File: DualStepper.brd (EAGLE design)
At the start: 53.1 x 63 mm, 14 parts

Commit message: Minor changes
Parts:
- moved ST1M1 0.81 mm to (55.8, 69.1)
- moved ST2M2 0.20 mm to (38.2, 68.9)
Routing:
- net N$3: track 25.9 -> 26.5 mm
- net N$4: track 29.2 -> 29.8 mm
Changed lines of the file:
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@@
 </element>
 <element name="SIGNAL" library="pinhead" package="1X04" value="" x="45.72" y="20.32"/>
-<element name="ST1M1" library="con-phoenix-350" package="1751248" value="1751248" x="54.9832" y="69.0614">
-<attribute name="OC_NEWARK" value="unknown" x="54.9832" y="69.0614" size="1.778" layer="27" display="off"/>
-<attribute name="MPN" value="" x="54.9832" y="69.0614" size="1.778" layer="27" display="off"/>
-<attribute name="MF" value="" x="54.9832" y="69.0614" size="1.778" layer="27" display="off"/>
-<attribute name="OC_FARNELL" value="unknown" x="54.9832" y="69.0614" size="1.778" layer="27" display="off"/>
+<element name="ST1M1" library="con-phoenix-350" package="1751248" value="1751248" x="55.796" y="69.0614">
+<attribute name="OC_NEWARK" value="unknown" x="55.796" y="69.0614" size="1.778" layer="27" display="off"/>
+<attribute name="MPN" value="" x="55.796" y="69.0614" size="1.778" layer="27" display="off"/>
+<attribute name="MF" value="" x="55.796" y="69.0614" size="1.778" layer="27" display="off"/>
+<attribute name="OC_FARNELL" value="unknown" x="55.796" y="69.0614" size="1.778" layer="27" display="off"/>
 </element>
 <element name="ST1M2" library="con-phoenix-350" package="1751248" value="1751248" x="63.3062" y="69.0614">
@@
 <attribute name="OC_FARNELL" value="unknown" x="30.7256" y="68.9598" size="1.778" layer="27" display="off"/>
 </element>
-<element name="ST2M2" library="con-phoenix-350" package="1751248" value="1751248" x="38.371" y="68.946">
-<attribute name="OC_NEWARK" value="unknown" x="38.371" y="68.946" size="1.778" layer="27" display="off"/>
-<attribute name="MPN" value="" x="38.371" y="68.946" size="1.778" layer="27" display="off"/>
-<attribute name="MF" value="" x="38.371" y="68.946" size="1.778" layer="27" display="off"/>
-<attribute name="OC_FARNELL" value="unknown" x="38.371" y="68.946" size="1.778" layer="27" display="off"/>
+<element name="ST2M2" library="con-phoenix-350" package="1751248" value="1751248" x="38.1678" y="68.946">
+<attribute name="OC_NEWARK" value="unknown" x="38.1678" y="68.946" size="1.778" layer="27" display="off"/>
+<attribute name="MPN" value="" x="38.1678" y="68.946" size="1.778" layer="27" display="off"/>
+<attribute name="MF" value="" x="38.1678" y="68.946" size="1.778" layer="27" display="off"/>
+<attribute name="OC_FARNELL" value="unknown" x="38.1678" y="68.946" size="1.778" layer="27" display="off"/>
 </element>
 <element name="VM" library="con-phoenix-350" package="1751248" value="1751248" x="46.6996" y="68.9852">
@@
 <contactref element="ST1M1" pad="2"/>
 <wire x1="54.6" y1="56.6" x2="54.6" y2="66.8282" width="0.8128" layer="16"/>
-<wire x1="54.6" y1="66.8282" x2="56.7332" y2="68.9614" width="0.8128" layer="16"/>
+<wire x1="54.6" y1="66.8282" x2="57.546" y2="68.9614" width="0.8128" layer="16"/>
 </signal>
 <signal name="N$4">
@@
 <contactref element="ST1M1" pad="1"/>
 <wire x1="53.34" y1="55.88" x2="53.34" y2="68.8546" width="0.8128" layer="16"/>
-<wire x1="53.34" y1="68.8546" x2="53.2332" y2="68.9614" width="0.8128" layer="16"/>
+<wire x1="53.34" y1="68.8546" x2="54.046" y2="68.9614" width="0.8128" layer="16"/>
 </signal>
 <signal name="N$12">
@@
 <contactref element="ST2M2" pad="1"/>
 <wire x1="39.37" y1="55.88" x2="39.37" y2="66.097" width="0.8128" layer="16"/>
-<wire x1="39.37" y1="66.097" x2="36.621" y2="68.846" width="0.8128" layer="16"/>
+<wire x1="39.37" y1="66.097" x2="36.4178" y2="68.846" width="0.8128" layer="16"/>
 </signal>
 <signal name="N$8">
@@
 <contactref element="ST2M2" pad="2"/>
 <wire x1="40.64" y1="57.15" x2="40.64" y2="68.327" width="0.8128" layer="16"/>
-<wire x1="40.64" y1="68.327" x2="40.121" y2="68.846" width="0.8128" layer="16"/>
+<wire x1="40.64" y1="68.327" x2="39.9178" y2="68.846" width="0.8128" layer="16"/>
 </signal>
 </signals>

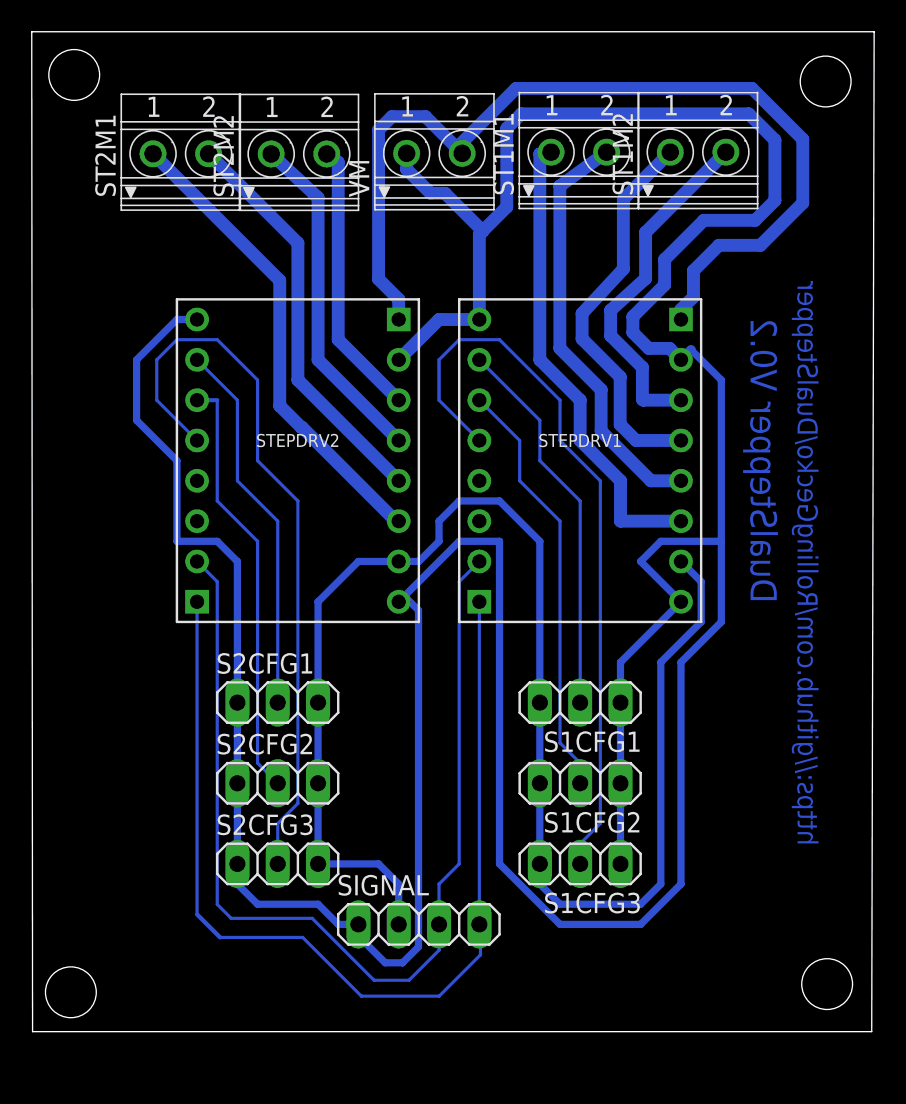
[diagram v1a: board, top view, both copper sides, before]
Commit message: Changed PWR connection position 2 Layer design GND Plate both sites Naming completed
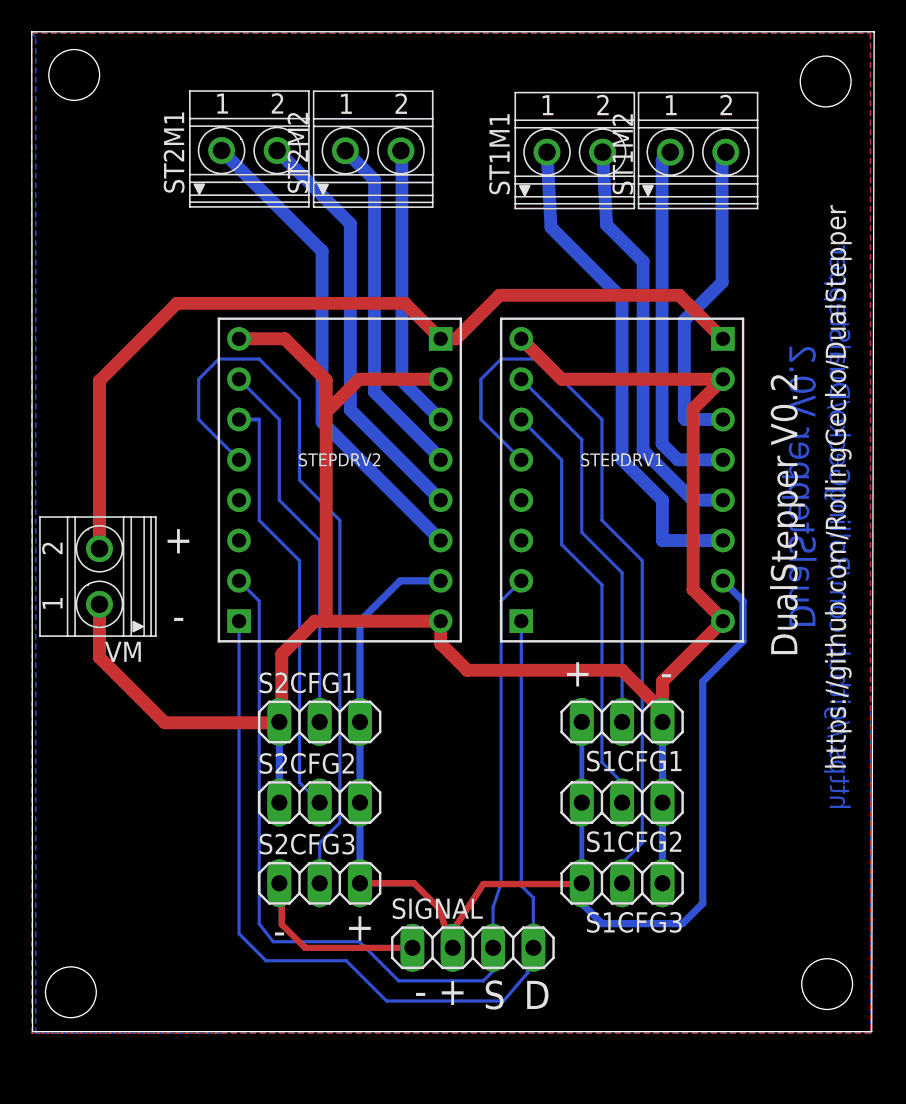
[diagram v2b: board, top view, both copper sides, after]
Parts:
- moved VM 34.1 mm to (25.5, 42.2), turned to 90 degrees
- moved ST2M2 4.68 mm to (42.8, 69.1)
- moved ST2M1 4.32 mm to (35.0, 69.2)
- moved SIGNAL 3.71 mm to (49.1, 18.8)
- moved S2CFG1 2.91 mm to (39.5, 33.1)
- moved S2CFG2 2.91 mm to (39.5, 28.0)
- moved S2CFG3 2.91 mm to (39.5, 22.9)
- moved S1CFG1 2.91 mm to (58.5, 33.1)
- moved S1CFG2 2.91 mm to (58.5, 28.0)
- moved S1CFG3 2.91 mm to (58.5, 22.9)
- moved STEPDRV1 2.91 mm to (58.5, 48.3)
- moved STEPDRV2 2.91 mm to (40.7, 48.3)
- moved ST1M1 0.25 mm to (55.5, 69.1)
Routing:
- net GND: track 250.5 -> 143.8 mm
- net +5V: track 105.4 -> 83.7 mm
- net +24V: track 59.8 -> 55.1 mm
- net N$2: track 24.6 -> 22.8 mm
- net N$1: track 21.9 -> 20.3 mm
- net N$4: track 29.8 -> 31.2 mm
- net N$6: track 25.6 -> 26.3 mm
- net N$5: track 29.7 -> 30.3 mm
- net N$16: track 64.4 -> 63.9 mm
- net N$7: track 21.4 -> 22.0 mm
- net N$8: track 17.5 -> 18.0 mm
- added copper zone on layer 1, net GND
- added copper zone on layer 16, net GND
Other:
- board text added: "+"
- board text added: "-"
- board text added: "D"
- board text added: "S"
